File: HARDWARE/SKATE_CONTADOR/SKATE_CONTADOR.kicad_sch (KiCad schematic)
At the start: 21 parts, among them J1 ENTRADA, J2 DISPLAY, SW1 INTERRUPTOR, SW2 VELOCIDAD, SW4 VELOCIDAD, U1 ESP32-DEVKIT-V1, U2 L7805

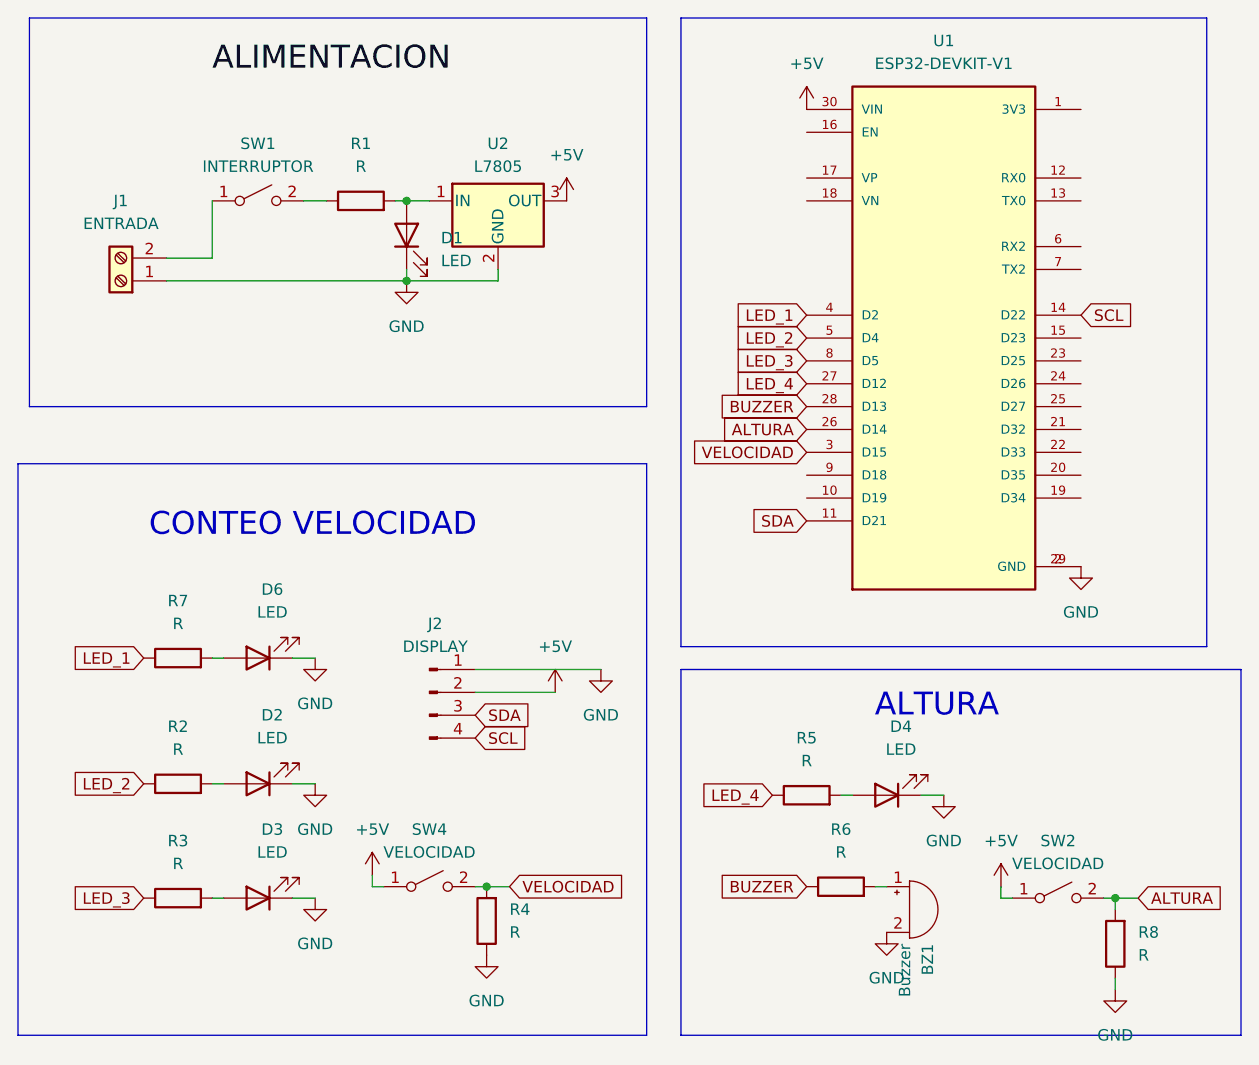
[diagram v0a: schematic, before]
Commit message: capacitores de filtro
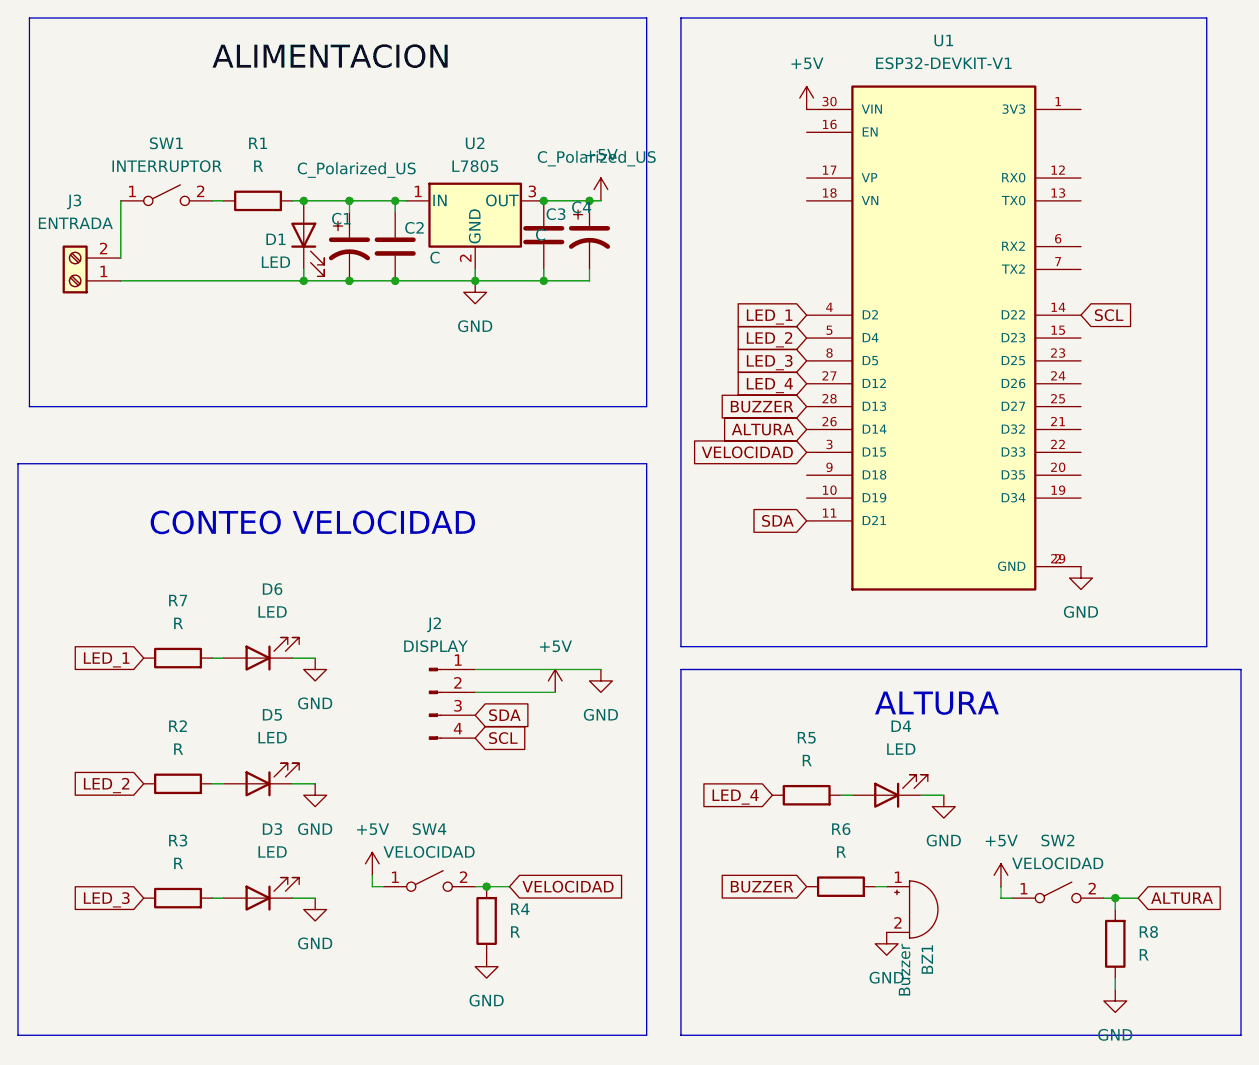
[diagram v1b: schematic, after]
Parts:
- removed D2: LED, Connector_PinHeader_2.54mm:PinHeader_1x02_P2.54mm_Vertical, symbol Device:LED
- removed J1: ENTRADA, TerminalBlock:TerminalBlock_bornier-2_P5.08mm, symbol Connector:Screw_Terminal_01x02
- added C1, C4: C_Polarized_US, Capacitor_THT:CP_Radial_D8.0mm_P5.00mm, symbol Device:C_Polarized_US
- added C2, C3: C, Capacitor_THT:C_Disc_D8.0mm_W2.5mm_P5.00mm, symbol Device:C
- added D5: LED, Connector_PinHeader_2.54mm:PinHeader_1x02_P2.54mm_Vertical, symbol Device:LED
- added J3: ENTRADA, TerminalBlock:TerminalBlock_bornier-2_P5.08mm, symbol Connector:Screw_Terminal_01x02
- BZ1: footprint Buzzer_Beeper:Buzzer_12x9.5RM7.6 -> Connector_PinHeader_2.54mm:PinHeader_1x02_P2.54mm_Vertical
- SW1: footprint Connector_PinSocket_2.54mm:PinSocket_1x02_P2.54mm_Vertical -> Button_Switch_THT:SW_Slide_SPDT_Angled_CK_OS102011MA1Q
- U2: footprint L7805:TO255P1020X450X2000-3 -> LM7805C:TO254P1011X419X2286-3
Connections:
- net +5V: now also C3.1, C4.1
- net GND: now also C1.2, C2.2, C3.2, C4.2, D5.1 (K), J3.1 (Pin_1)
- net at SW1.1 (A): now also J3.2 (Pin_2)
- net at D1.2 (A), R1.2, U2.1 (IN): now also C1.1, C2.1
- net at R2.2: now also D5.2 (A)
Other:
- moved on the sheet: D1, R1, SW1, U2
